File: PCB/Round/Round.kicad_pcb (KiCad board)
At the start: 2 copper layers, 70 x 70 mm, 55 parts, among them J3 Conn, SW1 ESE13V01D, U1 PN532, U2 QR, Y1 27.12MHz

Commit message: Cleaner edge
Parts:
- moved V1 0.22 mm to (100.0, 77.1)
- moved V2 0.08 mm to (100.0, 122.9)
- moved V3 0.08 mm to (77.1, 100.0)
- moved V4 0.08 mm to (122.9, 100.0)

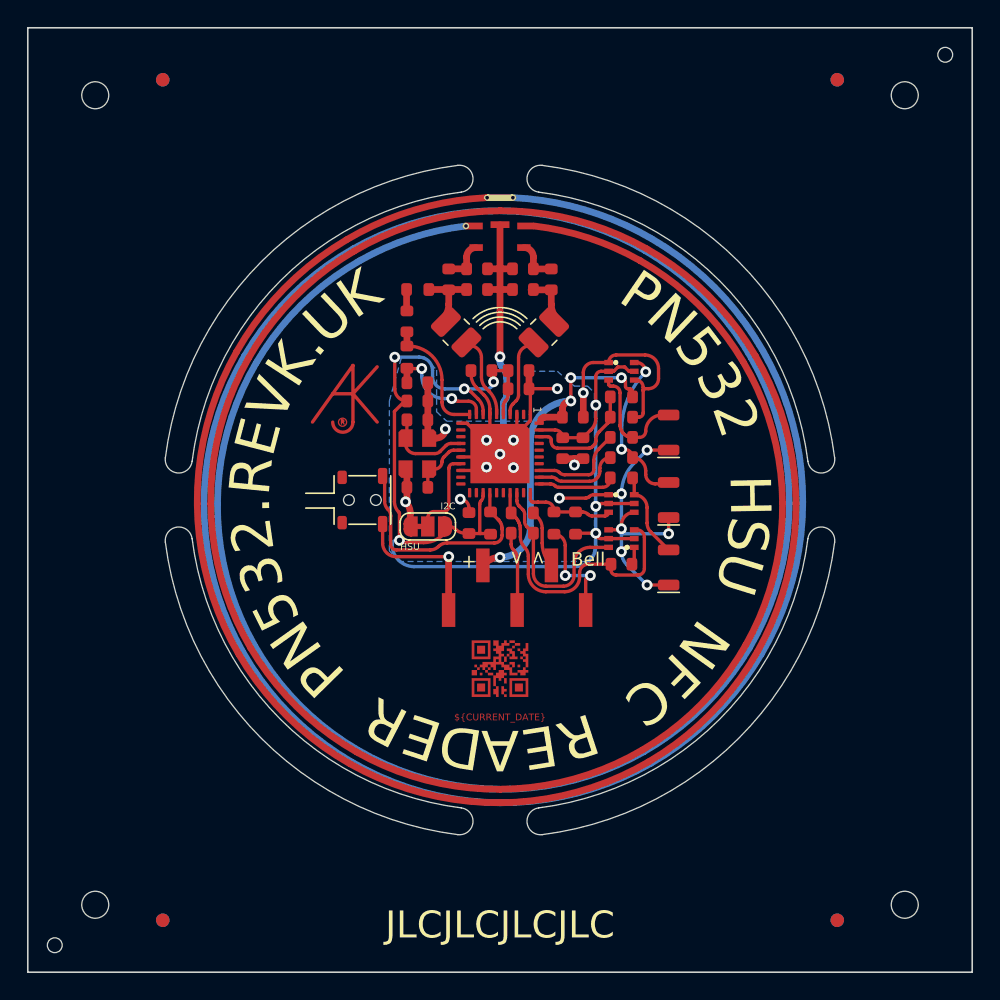
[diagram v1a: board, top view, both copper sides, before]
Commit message: Tidy and new ESP diodes
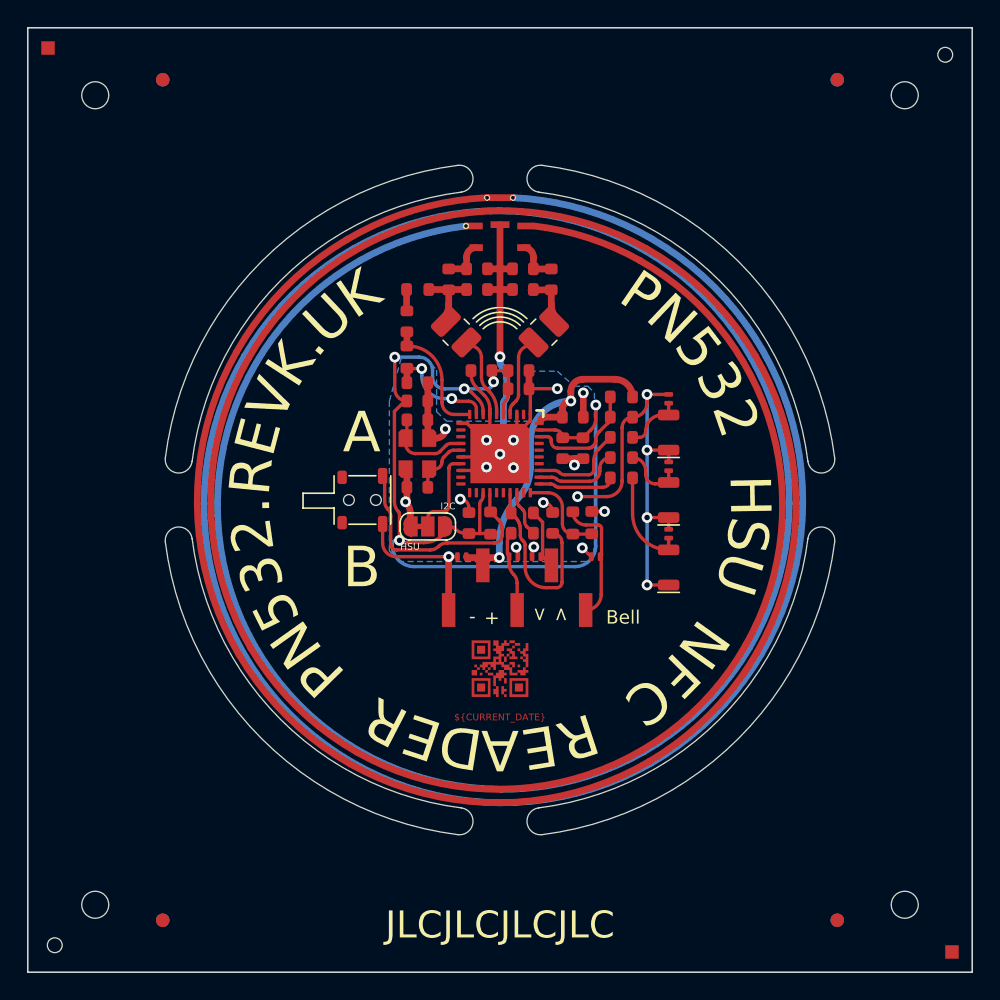
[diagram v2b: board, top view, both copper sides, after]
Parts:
- removed AJK1: AJK, RevK:AJK
- added D10: ~, RevK:DFN1006-2L, F.Cu at (97.2, 104.2)
- added D7: ~, RevK:DFN1006-2L, F.Cu at (112.5, 92.5)
- added D8: ~, RevK:DFN1006-2L, F.Cu at (101.0, 104.2)
- added D9: ~, RevK:DFN1006-2L, F.Cu at (102.7, 104.2)
- D4, D5, D6: value BAV99S -> ~; footprint RevK:SOT-363_SC-70-6 -> RevK:DFN1006-2L
- moved D5 7.86 mm to (112.5, 97.5), turned to 90 degrees
- moved C19 5.95 mm to (103.9, 101.7), turned to 90 degrees
- moved D4 4.16 mm to (112.5, 102.5), turned to 90 degrees
- moved D6 2.32 mm to (107.1, 104.2)
- moved R12 1.40 mm to (105.4, 101.7)
- moved R15 1.20 mm to (106.8, 101.7), turned to -90 degrees
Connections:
- C10 pad 1: +3V3 -> +3.3V
- C11 pad 1: +3V3 -> +3.3V
- C12 pad 1: +3V3 -> +3.3V
- C13 pad 1: +3V3 -> +3.3V
- C15 pad 1: +3V3 -> +3.3V
- C18 pad 1: +3V3 -> +3.3V
- C19 pad 1: Net-(D6B-K1A2) -> Net-(U1-NSS/P50_SCL/HSU_RX)
- C7 pad 1: +3V3 -> +3.3V
- D4 pad 1: GND -> Net-(D1-A)
- D4 pad 2: +3V3 -> GND
- D5 pad 1: GND -> Net-(D2-A)
- D5 pad 2: +3V3 -> GND
- D6 pad 1: GND -> Net-(J3-Pin_5)
- D6 pad 2: +3V3 -> GND
- JP1 pad 3: +3V3 -> +3.3V
- R11 pad 1: +3V3 -> +3.3V
- R12 pad 1: Net-(D4B-K1A2) -> Net-(J3-Pin_5)
- R12 pad 2: Net-(J3-Pin_5) -> Net-(U1-SCK/P72)
- R13 pad 2: Net-(D6A-K3A4) -> Net-(U1-MOSI/SDA/HSU_TX)
- R14 pad 2: Net-(D6B-K1A2) -> Net-(U1-NSS/P50_SCL/HSU_RX)
- R15 pad 1: +3V3 -> +3.3V
- R15 pad 2: Net-(D4B-K1A2) -> Net-(U1-SCK/P72)
- U1 pad 23: +3V3 -> +3.3V
- U1 pad 27: Net-(D6B-K1A2) -> Net-(U1-NSS/P50_SCL/HSU_RX)
- U1 pad 28: Net-(D6A-K3A4) -> Net-(U1-MOSI/SDA/HSU_TX)
- U1 pad 30: Net-(D4B-K1A2) -> Net-(U1-SCK/P72)
- U1 pad 39: +3V3 -> +3.3V
- U1 pad 5: +3V3 -> +3.3V
- U1 pad 8: +3V3 -> +3.3V
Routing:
- net +3V3: track 87.9 -> 0.00 mm, vias 7 -> 0
- net +3.3V: track 0.00 -> 76.8 mm, vias 0 -> 6
- net Net-(D6B-K1A2): track 20.8 -> 0.00 mm
- net Net-(D6A-K3A4): track 14.4 -> 0.00 mm
- net Net-(U1-NSS/P50_SCL/HSU_RX): track 0.00 -> 13.4 mm
- net Net-(D2-A): track 12.2 -> 4.70 mm, vias 2 -> 0
- net Net-(D4B-K1A2): track 6.93 -> 0.00 mm
- net Net-(U1-SCK/P72): track 0.00 -> 6.72 mm
- net GND: track 108.5 -> 103.1 mm, vias 20 -> 22
- net Net-(D3-A): track 8.11 -> 3.98 mm
- net Net-(U1-MOSI/SDA/HSU_TX): track 0.00 -> 3.43 mm
- net Net-(J3-Pin_5): track 8.11 -> 9.50 mm, vias 2 -> 0
- net Net-(D1-A): track 6.34 -> 7.63 mm
- net +5V: track 25.9 -> 26.0 mm, vias 4 -> 2
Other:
- board text added: "A"
- board text added: "B"

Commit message: Tidy
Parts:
- added C20: 100uF 6.3V, RevK:C_1206, F.Cu at (105.3, 92.3)
- moved R6 1.54 mm to (109.0, 93.9)
- moved R7 1.24 mm to (109.0, 95.1)
- moved R10 0.94 mm to (109.0, 96.3)
- moved R9 0.64 mm to (109.0, 97.5)
- moved R8 0.34 mm to (109.0, 98.7)
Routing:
- net GND: track 103.1 -> 99.3 mm
- net +3.3V: track 76.8 -> 73.6 mm
- net +5V: track 26.0 -> 24.6 mm
- net Net-(U1-RSTPD_N): track 8.64 -> 7.37 mm
- net Net-(D3-A): track 3.98 -> 5.11 mm
- net Net-(U1-P33_INT1): track 7.17 -> 6.62 mm
- added copper zone on F.Cu, net GND

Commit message: Tweak
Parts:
- moved D9 0.30 mm to (102.5, 104.0), turned to -90 degrees
- moved D8 0.28 mm to (100.8, 104.0), turned to 90 degrees
- moved D10 0.23 mm to (97.4, 104.2)
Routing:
- net GND: track 99.3 -> 108.2 mm
